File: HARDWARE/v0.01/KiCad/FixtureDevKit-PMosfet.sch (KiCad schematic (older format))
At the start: 56 parts, among them J63 FET_0, J64 FET_0, J65 FET_0, J66 FET_0, J67 FET_0, J68 FET_0, J69 FET_0, J70 FET_0, Q10 NTF2955T1G, Q11 NTF2955T1G, Q12 NTF2955T1G, Q5 NTF2955T1G, Q6 NTF2955T1G, Q7 NTF2955T1G, Q8 NTF2955T1G, Q9 NTF2955T1G

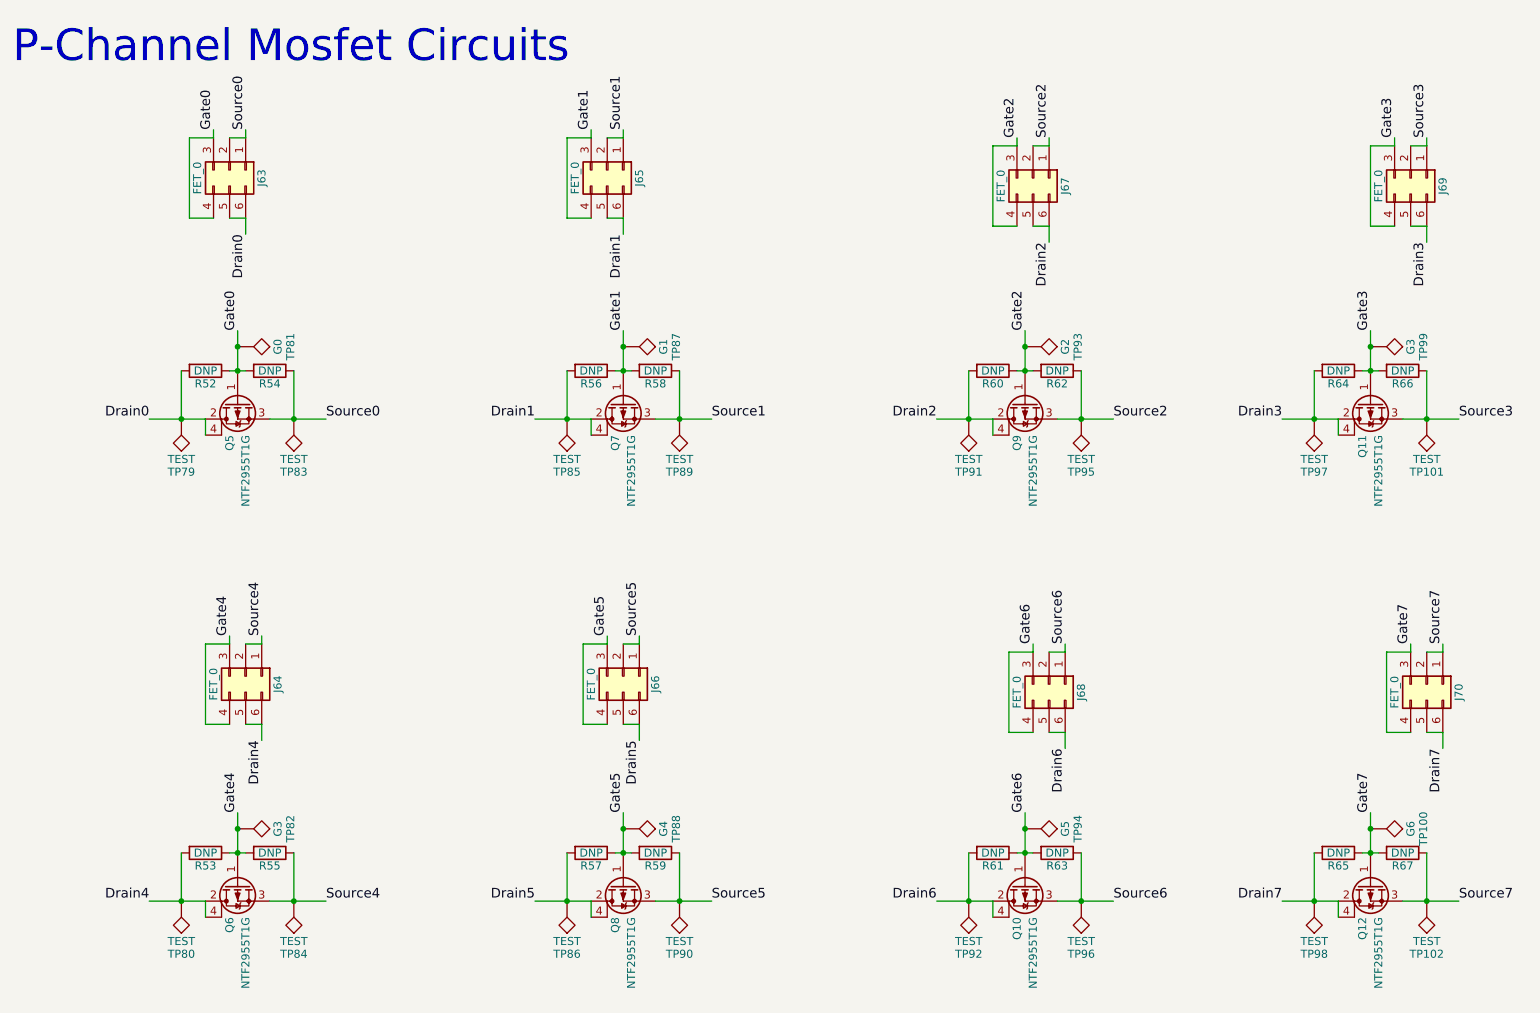
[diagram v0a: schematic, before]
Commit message: quasi-redoing entire schematic and layout
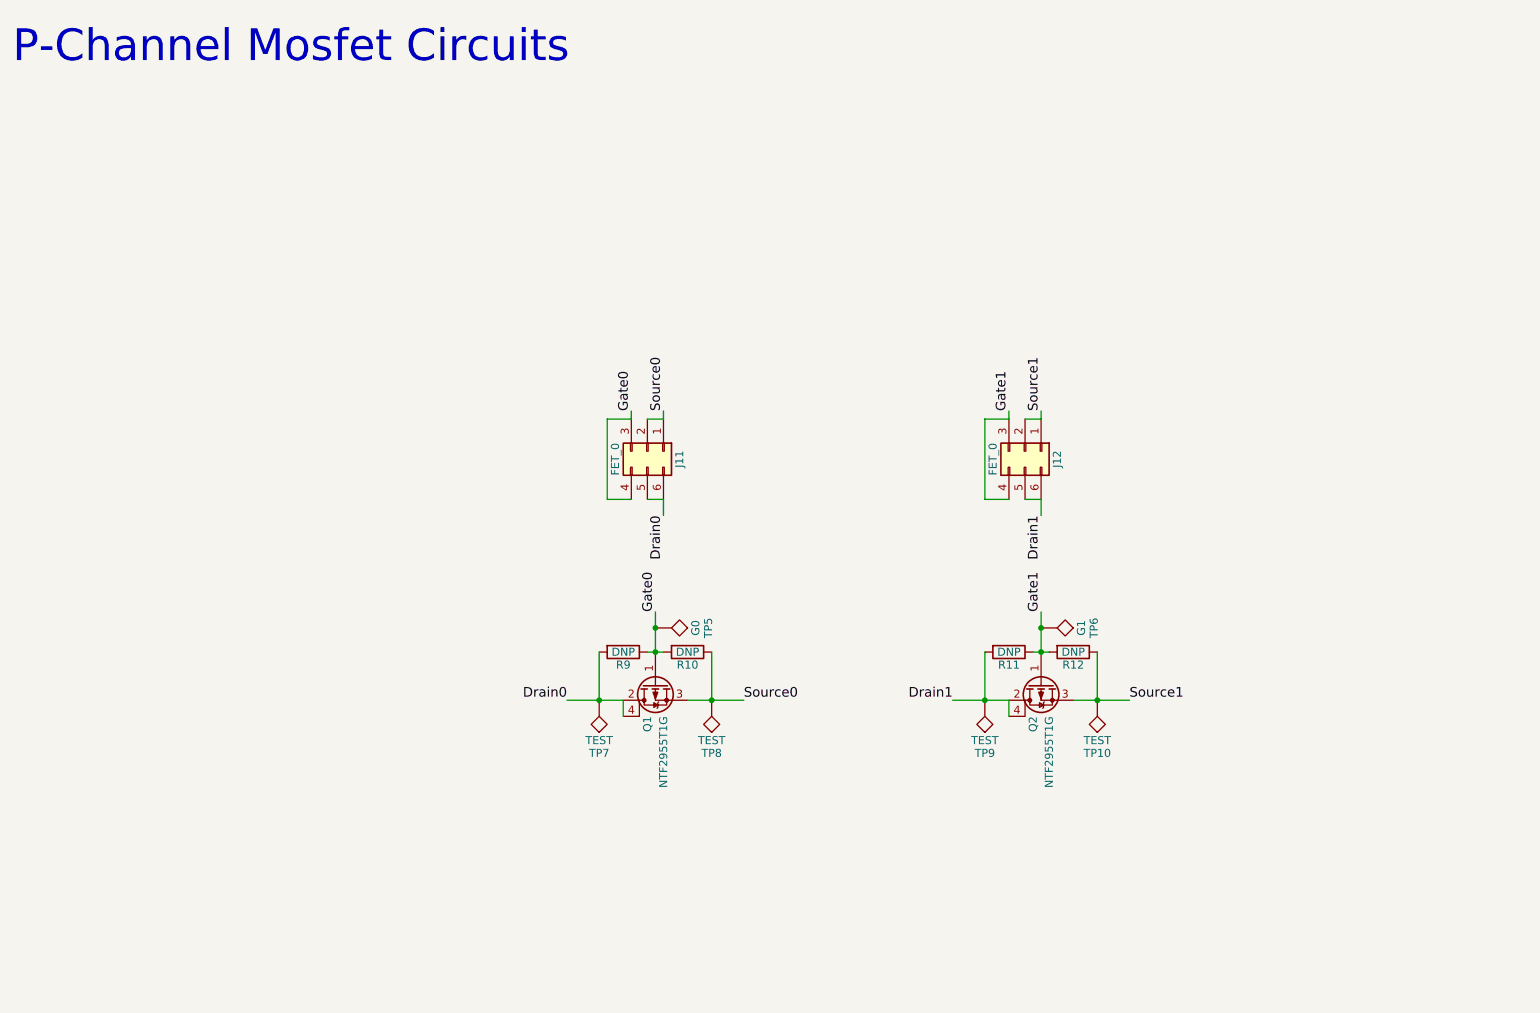
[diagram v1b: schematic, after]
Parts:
- removed J64, J66, J67, J68, J69, J70: FET_0, Pin_Headers:Pin_Header_Straight_2x03_Pitch2.54mm, symbol Conn_02x03_Counter_Clockwise
- removed Q10, Q11, Q12, Q6, Q8, Q9: NTF2955T1G, TO_SOT_Packages_SMD:SOT-223, symbol Q_PMOS_GDSD
- removed R53, R55, R57, R59, R60, R61, R62, R63, R64, R65, R66, R67: DNP, Resistors_SMD:R_0805_HandSoldering, symbol R
- removed TP100: G6, TestPoint:TestPoint, symbol TEST
- removed TP101, TP102, TP80, TP84, TP86, TP90, TP91, TP92, TP95, TP96, TP97, TP98: TEST, TestPoint:TestPoint, symbol TEST
- removed TP82, TP99: G3, TestPoint:TestPoint, symbol TEST
- removed TP88: G4, TestPoint:TestPoint, symbol TEST
- removed TP93: G2, TestPoint:TestPoint, symbol TEST
- removed TP94: G5, TestPoint:TestPoint, symbol TEST
- renumbered J63 to J11, J65 to J12, Q5 to Q1, Q7 to Q2, R54 to R10, R56 to R11, R58 to R12, R52 to R9, TP89 to TP10, TP81 to TP5, TP87 to TP6, TP79 to TP7, TP83 to TP8, TP85 to TP9
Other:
- moved on the sheet: J11, J12, Q1, Q2, R10, R11, R12, R9, TP10, TP5, TP6, TP7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
